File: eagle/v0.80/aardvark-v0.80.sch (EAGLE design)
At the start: 27 parts, among them IC1 LM1117-3.3, J1 MINI, U1 CH340C

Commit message: eagle/v0.80 updated schematic todo list
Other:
- note added: "TODO 1) Switch pushbutton switches 2) Shorten C3 slot?"
- note removed: "TODO 1) Update SLG47004V-DIP library or use Dialog? 2) Esthetics 3) Shorten C3 slot"
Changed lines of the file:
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@@
 <circle x="93.98" y="50.8" radius="1.27" width="0.1524" layer="94"/>
 <text x="182.88" y="58.42" size="2.54" layer="94">TODO
-1) Update SLG47004V-DIP library or use
-Dialog?
-2) Esthetics
-3) Shorten C3 slot</text>
+1) Switch pushbutton switches
+2) Shorten C3 slot?</text>
 </plain>
 <instances>

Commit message: eagle/v0.80/{*.brd,sch} added part numbers
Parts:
- C2: value 10uF -> 10uF 399-6674-1-ND
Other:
- note added: "TODO 1) Switch pushbutton switches 2) Shorten C3 slot? 3) Hole for USB connector tie wrap"
- note removed: "TODO 1) Switch pushbutton switches 2) Shorten C3 slot?"
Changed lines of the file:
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@@
 <part name="GND1" library="supply1" library_urn="urn:adsk.eagle:library:371" deviceset="GND" device=""/>
 <part name="FRAME1" library="apexprotofactory" deviceset="LETTER_L" device=""/>
-<part name="C2" library="rcl" library_urn="urn:adsk.eagle:library:334" deviceset="C-US" device="C0805" package3d_urn="urn:adsk.eagle:package:23617/2" value="10uF"/>
+<part name="C2" library="rcl" library_urn="urn:adsk.eagle:library:334" deviceset="C-US" device="C0805" package3d_urn="urn:adsk.eagle:package:23617/2" value="10uF 399-6674-1-ND"/>
 <part name="R1" library="rcl" library_urn="urn:adsk.eagle:library:334" deviceset="R-US_" device="R0805" package3d_urn="urn:adsk.eagle:package:23553/2" value="510"/>
 <part name="GND5" library="supply1" library_urn="urn:adsk.eagle:library:371" deviceset="GND" device=""/>
@@
 <text x="182.88" y="58.42" size="2.54" layer="94">TODO
 1) Switch pushbutton switches
-2) Shorten C3 slot?</text>
+2) Shorten C3 slot?
+3) Hole for USB connector tie wrap</text>
 </plain>
 <instances>

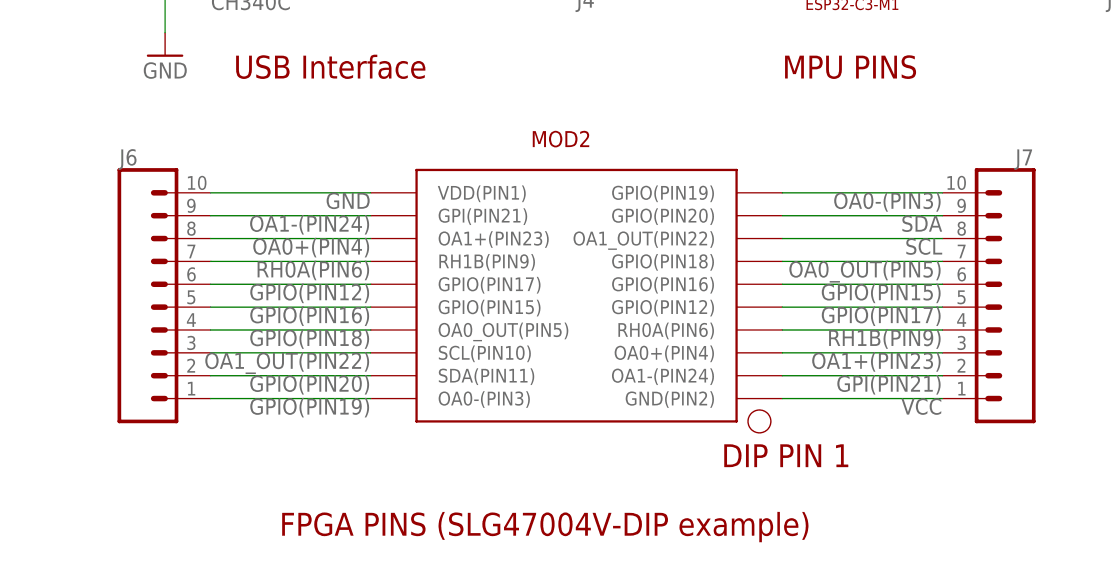
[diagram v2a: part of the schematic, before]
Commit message: fix pin connection mistake
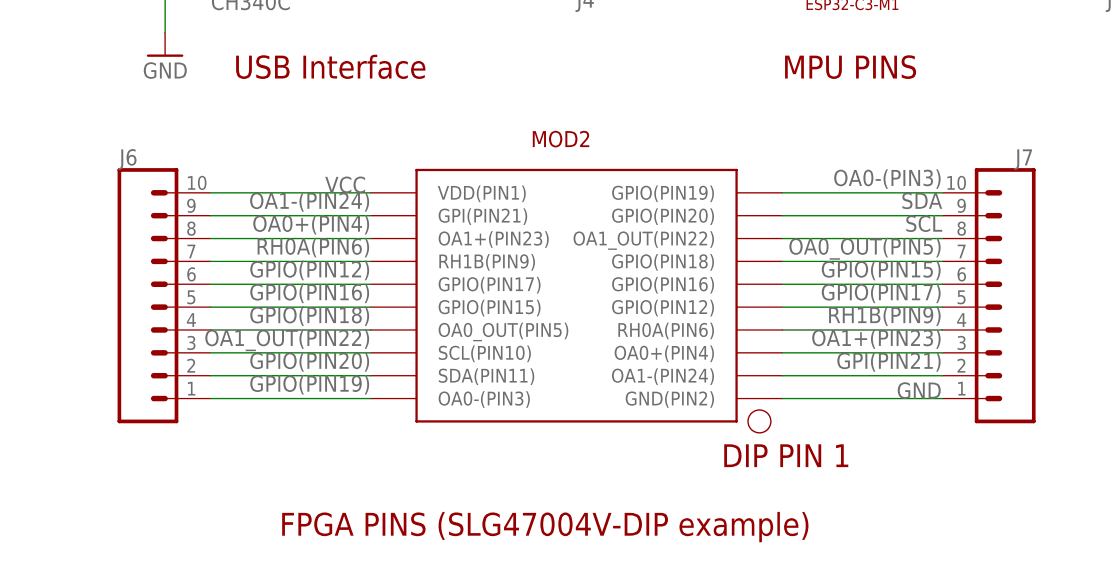
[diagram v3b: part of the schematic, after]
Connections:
- net GND: now also J7.1, MOD2.GND(PIN2); no longer J6.10, MOD2.VDD(PIN1)
- net VCC: now also J6.10, MOD2.VDD(PIN1); no longer J7.1, MOD2.GND(PIN2)
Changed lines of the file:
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@@
-</segment>
-<segment>
-<wire x1="114.3" y1="53.34" x2="96.52" y2="53.34" width="0.1524" layer="91"/>
-<label x="114.3" y="53.34" size="1.778" layer="95" rot="R180"/>
-<pinref part="MOD2" gate="FPGA1" pin="GND(PIN2)"/>
-<pinref part="J7" gate="J1" pin="1"/>
 </segment>
 <segment>
@@
 <label x="58.42" y="20.32" size="1.778" layer="95"/>
 <pinref part="J8" gate="J1" pin="2"/>
+</segment>
+<segment>
+<pinref part="J6" gate="J1" pin="10"/>
+<pinref part="MOD2" gate="FPGA1" pin="VDD(PIN1)"/>
+<wire x1="33.02" y1="76.2" x2="50.8" y2="76.2" width="0.1524" layer="91"/>
+<label x="45.72" y="76.2" size="1.778" layer="95"/>
 </segment>
 </net>
@@
 </segment>
 <segment>
-<wire x1="33.02" y1="76.2" x2="50.8" y2="76.2" width="0.1524" layer="91"/>
-<label x="50.8" y="76.2" size="1.778" layer="95" rot="R180"/>
-<pinref part="MOD2" gate="FPGA1" pin="VDD(PIN1)"/>
-<pinref part="J6" gate="J1" pin="10"/>
-</segment>
-<segment>
 <pinref part="R1" gate="G$1" pin="1"/>
 <wire x1="63.5" y1="139.7" x2="63.5" y2="137.16" width="0.1524" layer="91"/>
@@
 <junction x="116.84" y="139.7"/>
 </segment>
+<segment>
+<pinref part="MOD2" gate="FPGA1" pin="GND(PIN2)"/>
+<pinref part="J7" gate="J1" pin="1"/>
+<wire x1="96.52" y1="53.34" x2="114.3" y2="53.34" width="0.1524" layer="91"/>
+<label x="109.22" y="53.34" size="1.778" layer="95"/>
+</segment>
 </net>
 <net name="SCL" class="0">
 <segment>
 <wire x1="114.3" y1="71.12" x2="96.52" y2="71.12" width="0.1524" layer="91"/>
-<label x="114.3" y="71.12" size="1.778" layer="95" rot="R180"/>
+<label x="114.3" y="73.66" size="1.778" layer="95" rot="R180"/>
 <pinref part="MOD2" gate="FPGA1" pin="OA1_OUT(PIN22)"/>
 <pinref part="J7" gate="J1" pin="8"/>
@@
 <segment>
 <wire x1="114.3" y1="73.66" x2="96.52" y2="73.66" width="0.1524" layer="91"/>
-<label x="114.3" y="73.66" size="1.778" layer="95" rot="R180"/>
+<label x="114.3" y="76.2" size="1.778" layer="95" rot="R180"/>
 <pinref part="MOD2" gate="FPGA1" pin="GPIO(PIN20)"/>
 <pinref part="J7" gate="J1" pin="9"/>
@@
 <segment>
 <wire x1="33.02" y1="53.34" x2="50.8" y2="53.34" width="0.1524" layer="91"/>
-<label x="50.8" y="53.34" size="1.778" layer="95" rot="R180"/>
+<label x="50.8" y="55.88" size="1.778" layer="95" rot="R180"/>
 <pinref part="MOD2" gate="FPGA1" pin="OA0-(PIN3)"/>
 <pinref part="J6" gate="J1" pin="1"/>
@@
 <segment>
 <wire x1="33.02" y1="63.5" x2="50.8" y2="63.5" width="0.1524" layer="91"/>
-<label x="50.8" y="63.5" size="1.778" layer="95" rot="R180"/>
+<label x="50.8" y="66.04" size="1.778" layer="95" rot="R180"/>
 <pinref part="MOD2" gate="FPGA1" pin="GPIO(PIN15)"/>
 <pinref part="J6" gate="J1" pin="5"/>
@@
 <segment>
 <wire x1="33.02" y1="60.96" x2="50.8" y2="60.96" width="0.1524" layer="91"/>
-<label x="50.8" y="60.96" size="1.778" layer="95" rot="R180"/>
+<label x="50.8" y="63.5" size="1.778" layer="95" rot="R180"/>
 <pinref part="MOD2" gate="FPGA1" pin="OA0_OUT(PIN5)"/>
 <pinref part="J6" gate="J1" pin="4"/>
@@
 <segment>
 <wire x1="33.02" y1="58.42" x2="50.8" y2="58.42" width="0.1524" layer="91"/>
-<label x="50.8" y="58.42" size="1.778" layer="95" rot="R180"/>
+<label x="50.8" y="60.96" size="1.778" layer="95" rot="R180"/>
 <pinref part="MOD2" gate="FPGA1" pin="SCL(PIN10)"/>
 <pinref part="J6" gate="J1" pin="3"/>
@@
 <segment>
 <wire x1="33.02" y1="66.04" x2="50.8" y2="66.04" width="0.1524" layer="91"/>
-<label x="50.8" y="66.04" size="1.778" layer="95" rot="R180"/>
+<label x="50.8" y="68.58" size="1.778" layer="95" rot="R180"/>
 <pinref part="MOD2" gate="FPGA1" pin="GPIO(PIN17)"/>
 <pinref part="J6" gate="J1" pin="6"/>
@@
 <segment>
 <wire x1="114.3" y1="60.96" x2="96.52" y2="60.96" width="0.1524" layer="91"/>
-<label x="114.3" y="60.96" size="1.778" layer="95" rot="R180"/>
+<label x="114.3" y="63.5" size="1.778" layer="95" rot="R180"/>
 <pinref part="MOD2" gate="FPGA1" pin="RH0A(PIN6)"/>
 <pinref part="J7" gate="J1" pin="4"/>
@@
 <segment>
 <wire x1="33.02" y1="55.88" x2="50.8" y2="55.88" width="0.1524" layer="91"/>
-<label x="50.8" y="55.88" size="1.778" layer="95" rot="R180"/>
+<label x="50.8" y="58.42" size="1.778" layer="95" rot="R180"/>
 <pinref part="MOD2" gate="FPGA1" pin="SDA(PIN11)"/>
 <pinref part="J6" gate="J1" pin="2"/>
@@
 <segment>
 <wire x1="114.3" y1="63.5" x2="96.52" y2="63.5" width="0.1524" layer="91"/>
-<label x="114.3" y="63.5" size="1.778" layer="95" rot="R180"/>
+<label x="114.3" y="66.04" size="1.778" layer="95" rot="R180"/>
 <pinref part="MOD2" gate="FPGA1" pin="GPIO(PIN12)"/>
 <pinref part="J7" gate="J1" pin="5"/>
@@
 <segment>
 <wire x1="114.3" y1="66.04" x2="96.52" y2="66.04" width="0.1524" layer="91"/>
-<label x="114.3" y="66.04" size="1.778" layer="95" rot="R180"/>
+<label x="114.3" y="68.58" size="1.778" layer="95" rot="R180"/>
 <pinref part="MOD2" gate="FPGA1" pin="GPIO(PIN16)"/>
 <pinref part="J7" gate="J1" pin="6"/>
@@
 <segment>
 <wire x1="114.3" y1="68.58" x2="96.52" y2="68.58" width="0.1524" layer="91"/>
-<label x="114.3" y="68.58" size="1.778" layer="95" rot="R180"/>
+<label x="114.3" y="71.12" size="1.778" layer="95" rot="R180"/>
 <pinref part="MOD2" gate="FPGA1" pin="GPIO(PIN18)"/>
 <pinref part="J7" gate="J1" pin="7"/>
@@
 <segment>
 <wire x1="114.3" y1="76.2" x2="96.52" y2="76.2" width="0.1524" layer="91"/>
-<label x="114.3" y="76.2" size="1.778" layer="95" rot="R180"/>
+<label x="114.3" y="78.74" size="1.778" layer="95" rot="R180"/>
 <pinref part="MOD2" gate="FPGA1" pin="GPIO(PIN19)"/>
 <pinref part="J7" gate="J1" pin="10"/>
@@
 <segment>
 <wire x1="114.3" y1="55.88" x2="96.52" y2="55.88" width="0.1524" layer="91"/>
-<label x="114.3" y="55.88" size="1.778" layer="95" rot="R180"/>
+<label x="114.3" y="58.42" size="1.778" layer="95" rot="R180"/>
 <pinref part="MOD2" gate="FPGA1" pin="OA1-(PIN24)"/>
 <pinref part="J7" gate="J1" pin="2"/>
@@
 <segment>
 <wire x1="114.3" y1="58.42" x2="96.52" y2="58.42" width="0.1524" layer="91"/>
-<label x="114.3" y="58.42" size="1.778" layer="95" rot="R180"/>
+<label x="114.3" y="60.96" size="1.778" layer="95" rot="R180"/>
 <pinref part="MOD2" gate="FPGA1" pin="OA0+(PIN4)"/>
 <pinref part="J7" gate="J1" pin="3"/>
@@
 <segment>
 <wire x1="33.02" y1="71.12" x2="50.8" y2="71.12" width="0.1524" layer="91"/>
-<label x="50.8" y="71.12" size="1.778" layer="95" rot="R180"/>
+<label x="50.8" y="73.66" size="1.778" layer="95" rot="R180"/>
 <pinref part="MOD2" gate="FPGA1" pin="OA1+(PIN23)"/>
 <pinref part="J6" gate="J1" pin="8"/>
@@
 <segment>
 <wire x1="33.02" y1="73.66" x2="50.8" y2="73.66" width="0.1524" layer="91"/>
-<label x="50.8" y="73.66" size="1.778" layer="95" rot="R180"/>
+<label x="50.8" y="76.2" size="1.778" layer="95" rot="R180"/>
 <pinref part="MOD2" gate="FPGA1" pin="GPI(PIN21)"/>
 <pinref part="J6" gate="J1" pin="9"/>
@@
 <segment>
 <wire x1="33.02" y1="68.58" x2="50.8" y2="68.58" width="0.1524" layer="91"/>
-<label x="50.8" y="68.58" size="1.778" layer="95" rot="R180"/>
+<label x="50.8" y="71.12" size="1.778" layer="95" rot="R180"/>
 <pinref part="MOD2" gate="FPGA1" pin="RH1B(PIN9)"/>
 <pinref part="J6" gate="J1" pin="7"/>
